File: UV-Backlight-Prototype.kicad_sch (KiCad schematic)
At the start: 82 parts, among them J1 Conn_02x08_Odd_Even

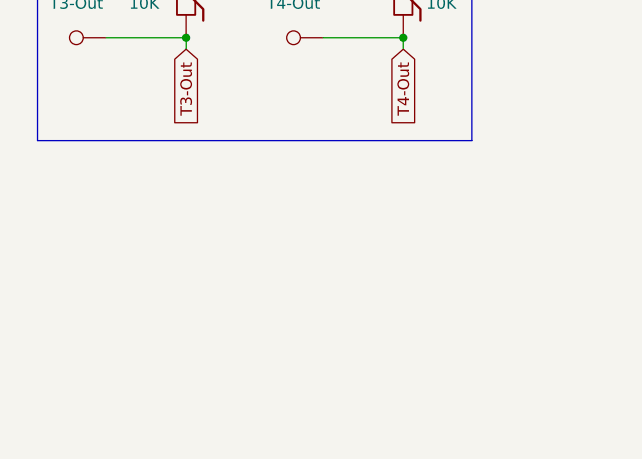
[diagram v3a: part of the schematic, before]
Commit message: Update UV-Backlight-Prototype.kicad_sch
Added Mounting holes to schematic. M3 mounting holes, connected to ground, vias around hole for aesthetics
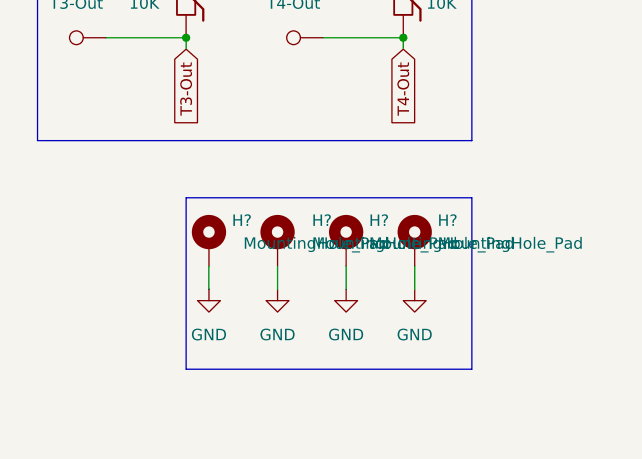
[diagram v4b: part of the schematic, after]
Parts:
- added H? (x3): MountingHole_Pad, MountingHole:MountingHole_3.2mm_M3_Pad_Via, symbol Mechanical:MountingHole_Pad
- added H?: MountingHole_Pad, symbol Mechanical:MountingHole_Pad
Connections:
- new net GND: H?.1, H?.1, H?.1, H?.1
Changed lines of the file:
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@@
+    (stroke (width 0) (type default) (color 0 0 0 0))
+  )
+  (wire (pts (xy 255.27 139.7) (xy 255.27 142.24))
     (stroke (width 0) (type default) (color 0 0 0 0))
   )
@@
     (stroke (width 0) (type default) (color 0 0 0 0))
   )
+  (polyline (pts (xy 261.62 132.08) (xy 261.62 151.13))
+    (stroke (width 0) (type default) (color 0 0 0 0))
+  )
   (wire (pts (xy 229.87 40.64) (xy 237.49 40.64))
     (stroke (width 0) (type default) (color 0 0 0 0))
@@
     (stroke (width 0) (type default) (color 0 0 0 0))
   )
+  (polyline (pts (xy 229.87 132.08) (xy 229.87 151.13))
+    (stroke (width 0) (type default) (color 0 0 0 0))
+  )
   (wire (pts (xy 97.79 53.34) (xy 97.79 55.88))
     (stroke (width 0) (type default) (color 0 0 0 0))
@@
     (stroke (width 0) (type default) (color 0 0 0 0))
   )
+  (wire (pts (xy 232.41 139.7) (xy 232.41 142.24))
+    (stroke (width 0) (type default) (color 0 0 0 0))
+  )
   (polyline (pts (xy 213.36 57.15) (xy 261.62 57.15))
     (stroke (width 0) (type default) (color 0 0 0 0))
@@
     (stroke (width 0) (type default) (color 0 0 0 0))
   )
+  (wire (pts (xy 240.03 139.7) (xy 240.03 142.24))
+    (stroke (width 0) (type default) (color 0 0 0 0))
+  )
   (wire (pts (xy 149.86 123.19) (xy 151.13 123.19))
     (stroke (width 0) (type default) (color 0 0 0 0))
@@
     (stroke (width 0) (type default) (color 0 0 0 0))
   )
+  (wire (pts (xy 247.65 139.7) (xy 247.65 142.24))
+    (stroke (width 0) (type default) (color 0 0 0 0))
+  )
   (wire (pts (xy 44.45 107.95) (xy 44.45 109.22))
     (stroke (width 0) (type default) (color 0 0 0 0))
@@
     (stroke (width 0) (type default) (color 0 0 0 0))
   )
+  (polyline (pts (xy 261.62 151.13) (xy 229.87 151.13))
+    (stroke (width 0) (type default) (color 0 0 0 0))
+  )
   (polyline (pts (xy 261.62 57.15) (xy 261.62 125.73))
     (stroke (width 0) (type default) (color 0 0 0 0))
@@
   )
   (polyline (pts (xy 274.32 54.61) (xy 213.36 54.61))
+    (stroke (width 0) (type default) (color 0 0 0 0))
+  )
+  (polyline (pts (xy 229.87 132.08) (xy 261.62 132.08))
     (stroke (width 0) (type default) (color 0 0 0 0))
   )
@@
     (pin "1")
   )
+  (symbol (lib_id "power:GND") (at 255.27 142.24 0) (unit 1)
+    (in_bom yes) (on_board yes) (fields_autoplaced)
+    (property "Reference" "#PWR?" (id 0) (at 255.27 148.59 0)
+      (effects (font (size 1.27 1.27)) hide)
+    )
+    (property "Value" "GND" (id 1) (at 255.27 147.32 0))
+    (property "Footprint" "" (id 2) (at 255.27 142.24 0)
+      (effects (font (size 1.27 1.27)) hide)
+    )
+    (property "Datasheet" "" (id 3) (at 255.27 142.24 0)
+      (effects (font (size 1.27 1.27)) hide)
+    )
+    (pin "1")
+  )
   (symbol (lib_id "Jumper:Jumper_2_Open") (at 142.24 33.02 0) (unit 1)
     (in_bom yes) (on_board yes)
@@
     (pin "2")
   )
+  (symbol (lib_id "Mechanical:MountingHole_Pad") (at 247.65 137.16 0) (unit 1)
+    (in_bom yes) (on_board yes) (fields_autoplaced)
+    (property "Reference" "H?" (id 0) (at 250.19 134.6199 0)
+      (effects (font (size 1.27 1.27)) (justify left))
+    )
+    (property "Value" "MountingHole_Pad" (id 1) (at 250.19 137.1599 0)
+      (effects (font (size 1.27 1.27)) (justify left))
+    )
+    (property "Footprint" "MountingHole:MountingHole_3.2mm_M3_Pad_Via" (id 2) (at 247.65 137.16 0)
+      (effects (font (size 1.27 1.27)) hide)
+    )
+    (property "Datasheet" "~" (id 3) (at 247.65 137.16 0)
+      (effects (font (size 1.27 1.27)) hide)
+    )
+    (pin "1")
+  )
   (symbol (lib_id "Jumper:Jumper_2_Open") (at 90.17 33.02 0) (unit 1)
     (in_bom yes) (on_board yes)
@@
     (pin "1")
   )
+  (symbol (lib_id "Mechanical:MountingHole_Pad") (at 255.27 137.16 0) (unit 1)
+    (in_bom yes) (on_board yes) (fields_autoplaced)
+    (property "Reference" "H?" (id 0) (at 257.81 134.6199 0)
+      (effects (font (size 1.27 1.27)) (justify left))
+    )
+    (property "Value" "MountingHole_Pad" (id 1) (at 257.81 137.1599 0)
+      (effects (font (size 1.27 1.27)) (justify left))
+    )
+    (property "Footprint" "MountingHole:MountingHole_3.2mm_M3_Pad_Via" (id 2) (at 255.27 137.16 0)
+      (effects (font (size 1.27 1.27)) hide)
+    )
+    (property "Datasheet" "~" (id 3) (at 255.27 137.16 0)
+      (effects (font (size 1.27 1.27)) hide)
+    )
+    (pin "1")
+  )
   (symbol (lib_id "Connector:TestPoint") (at 97.79 31.75 270) (unit 1)
     (in_bom yes) (on_board yes) (fields_autoplaced)
@@
     (pin "2")
   )
+  (symbol (lib_id "Mechanical:MountingHole_Pad") (at 232.41 137.16 0) (unit 1)
+    (in_bom yes) (on_board yes)
+    (property "Reference" "H?" (id 0) (at 234.95 134.6199 0)
+      (effects (font (size 1.27 1.27)) (justify left))
+    )
+    (property "Value" "MountingHole_Pad" (id 1) (at 236.22 137.1599 0)
+      (effects (font (size 1.27 1.27)) (justify left))
+    )
+    (property "Footprint" "" (id 2) (at 232.41 137.16 0)
+      (effects (font (size 1.27 1.27)) hide)
+    )
+    (property "Datasheet" "~" (id 3) (at 232.41 137.16 0)
+      (effects (font (size 1.27 1.27)) hide)
+    )
+    (pin "1")
+  )
   (symbol (lib_id "Connector:TestPoint") (at 151.13 93.98 270) (unit 1)
     (in_bom yes) (on_board yes) (fields_autoplaced)
@@
     (pin "2")
   )
+  (symbol (lib_id "power:GND") (at 240.03 142.24 0) (unit 1)
+    (in_bom yes) (on_board yes) (fields_autoplaced)
+    (property "Reference" "#PWR?" (id 0) (at 240.03 148.59 0)
+      (effects (font (size 1.27 1.27)) hide)
+    )
+    (property "Value" "GND" (id 1) (at 240.03 147.32 0))
+    (property "Footprint" "" (id 2) (at 240.03 142.24 0)
+      (effects (font (size 1.27 1.27)) hide)
+    )
+    (property "Datasheet" "" (id 3) (at 240.03 142.24 0)
+      (effects (font (size 1.27 1.27)) hide)
+    )
+    (pin "1")
+  )
   (symbol (lib_id "Connector:TestPoint") (at 245.11 81.28 90) (unit 1)
     (in_bom yes) (on_board yes) (fields_autoplaced)
@@
     (pin "2")
   )
+  (symbol (lib_id "power:GND") (at 232.41 142.24 0) (unit 1)
+    (in_bom yes) (on_board yes) (fields_autoplaced)
+    (property "Reference" "#PWR?" (id 0) (at 232.41 148.59 0)
+      (effects (font (size 1.27 1.27)) hide)
+    )
+    (property "Value" "GND" (id 1) (at 232.41 147.32 0))
+    (property "Footprint" "" (id 2) (at 232.41 142.24 0)
+      (effects (font (size 1.27 1.27)) hide)
+    )
+    (property "Datasheet" "" (id 3) (at 232.41 142.24 0)
+      (effects (font (size 1.27 1.27)) hide)
+    )
+    (pin "1")
+  )
   (symbol (lib_id "Device:LED") (at 44.45 102.87 90) (unit 1)
     (in_bom yes) (on_board yes) (fields_autoplaced)
@@
     (pin "1")
     (pin "2")
+  )
+  (symbol (lib_id "power:GND") (at 247.65 142.24 0) (unit 1)
+    (in_bom yes) (on_board yes) (fields_autoplaced)
+    (property "Reference" "#PWR?" (id 0) (at 247.65 148.59 0)
+      (effects (font (size 1.27 1.27)) hide)
+    )
+    (property "Value" "GND" (id 1) (at 247.65 147.32 0))
+    (property "Footprint" "" (id 2) (at 247.65 142.24 0)
+      (effects (font (size 1.27 1.27)) hide)
+    )
+    (property "Datasheet" "" (id 3) (at 247.65 142.24 0)
+      (effects (font (size 1.27 1.27)) hide)
+    )
+    (pin "1")
   )
   (symbol (lib_id "Connector:TestPoint") (at 151.13 106.68 270) (unit 1)
@@
     (pin "2")
   )
+  (symbol (lib_id "Mechanical:MountingHole_Pad") (at 240.03 137.16 0) (unit 1)
+    (in_bom yes) (on_board yes)
+    (property "Reference" "H?" (id 0) (at 243.84 134.6199 0)
+      (effects (font (size 1.27 1.27)) (justify left))
+    )
+    (property "Value" "MountingHole_Pad" (id 1) (at 243.84 137.1599 0)
+      (effects (font (size 1.27 1.27)) (justify left))
+    )
+    (property "Footprint" "MountingHole:MountingHole_3.2mm_M3_Pad_Via" (id 2) (at 240.03 137.16 0)
+      (effects (font (size 1.27 1.27)) hide)
+    )
+    (property "Datasheet" "~" (id 3) (at 240.03 137.16 0)
+      (effects (font (size 1.27 1.27)) hide)
+    )
+    (pin "1")
+  )
   (symbol (lib_id "Connector:TestPoint") (at 220.98 71.12 90) (unit 1)
     (in_bom yes) (on_board yes) (fields_autoplaced)
@@
   )
   (symbol_instances
+    (path "/1281690f-d0c0-4e7c-8e9b-b3fec11a3e67"
+      (reference "#PWR?") (unit 1) (value "GND") (footprint "")
+    )
+    (path "/9259b80d-1969-4589-94a9-080673952826"
+      (reference "#PWR?") (unit 1) (value "GND") (footprint "")
+    )
+    (path "/a3a27186-2051-4909-991d-caf80cec8df9"
+      (reference "#PWR?") (unit 1) (value "GND") (footprint "")
+    )
+    (path "/bb1469d3-6926-4d46-adfc-865ef7215321"
+      (reference "#PWR?") (unit 1) (value "GND") (footprint "")
+    )
     (path "/dce51636-b20e-418f-aae8-16711401d173"
       (reference "D1") (unit 1) (value "UV LED") (footprint "LED_SMD:LED_PLCC_2835_Handsoldering")
@@
       (reference "D21") (unit 1) (value "UV LED") (footprint "LED_SMD:LED_PLCC_2835_Handsoldering")
     )
+    (path "/358db39b-417f-4d50-8276-ae73a4dbda31"
+      (reference "H?") (unit 1) (value "MountingHole_Pad") (footprint "MountingHole:MountingHole_3.2mm_M3_Pad_Via")
+    )
+    (path "/40150b75-969d-4cd4-93e5-e8258fa7d188"
+      (reference "H?") (unit 1) (value "MountingHole_Pad") (footprint "MountingHole:MountingHole_3.2mm_M3_Pad_Via")
+    )
+    (path "/757c54d8-07ff-441d-be3d-65751b9d4914"
+      (reference "H?") (unit 1) (value "MountingHole_Pad") (footprint "MountingHole:MountingHole_3.2mm_M3_Pad_Via")
+    )
+    (path "/e24b16b7-83bf-4189-99e5-84cfc419f98d"
+      (reference "H?") (unit 1) (value "MountingHole_Pad") (footprint "MountingHole:MountingHole_3.2mm_M3_Pad_Via")
+    )
     (path "/c36a3340-352f-453e-a7ed-e92b15cd9612"

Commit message: Autosave
autosave
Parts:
- gave numbers to parts that had none: 4
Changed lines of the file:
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@@
   (symbol (lib_id "power:GND") (at 255.27 142.24 0) (unit 1)
     (in_bom yes) (on_board yes) (fields_autoplaced)
-    (property "Reference" "#PWR?" (id 0) (at 255.27 148.59 0)
+    (property "Reference" "#PWR04" (id 0) (at 255.27 148.59 0)
       (effects (font (size 1.27 1.27)) hide)
     )
@@
   (symbol (lib_id "Mechanical:MountingHole_Pad") (at 247.65 137.16 0) (unit 1)
     (in_bom yes) (on_board yes) (fields_autoplaced)
-    (property "Reference" "H?" (id 0) (at 250.19 134.6199 0)
+    (property "Reference" "H3" (id 0) (at 250.19 134.6199 0)
       (effects (font (size 1.27 1.27)) (justify left))
     )
@@
   (symbol (lib_id "Mechanical:MountingHole_Pad") (at 255.27 137.16 0) (unit 1)
     (in_bom yes) (on_board yes) (fields_autoplaced)
-    (property "Reference" "H?" (id 0) (at 257.81 134.6199 0)
+    (property "Reference" "H4" (id 0) (at 257.81 134.6199 0)
       (effects (font (size 1.27 1.27)) (justify left))
     )
@@
   (symbol (lib_id "Mechanical:MountingHole_Pad") (at 232.41 137.16 0) (unit 1)
     (in_bom yes) (on_board yes)
-    (property "Reference" "H?" (id 0) (at 234.95 134.6199 0)
+    (property "Reference" "H1" (id 0) (at 234.95 134.6199 0)
       (effects (font (size 1.27 1.27)) (justify left))
     )
@@
   (symbol (lib_id "power:GND") (at 240.03 142.24 0) (unit 1)
     (in_bom yes) (on_board yes) (fields_autoplaced)
-    (property "Reference" "#PWR?" (id 0) (at 240.03 148.59 0)
+    (property "Reference" "#PWR02" (id 0) (at 240.03 148.59 0)
       (effects (font (size 1.27 1.27)) hide)
     )
@@
   (symbol (lib_id "power:GND") (at 232.41 142.24 0) (unit 1)
     (in_bom yes) (on_board yes) (fields_autoplaced)
-    (property "Reference" "#PWR?" (id 0) (at 232.41 148.59 0)
+    (property "Reference" "#PWR01" (id 0) (at 232.41 148.59 0)
       (effects (font (size 1.27 1.27)) hide)
     )
@@
   (symbol (lib_id "power:GND") (at 247.65 142.24 0) (unit 1)
     (in_bom yes) (on_board yes) (fields_autoplaced)
-    (property "Reference" "#PWR?" (id 0) (at 247.65 148.59 0)
+    (property "Reference" "#PWR03" (id 0) (at 247.65 148.59 0)
       (effects (font (size 1.27 1.27)) hide)
     )
@@
   (symbol (lib_id "Mechanical:MountingHole_Pad") (at 240.03 137.16 0) (unit 1)
     (in_bom yes) (on_board yes)
-    (property "Reference" "H?" (id 0) (at 243.84 134.6199 0)
+    (property "Reference" "H2" (id 0) (at 243.84 134.6199 0)
       (effects (font (size 1.27 1.27)) (justify left))
     )
@@
   )
   (symbol_instances
+    (path "/a3a27186-2051-4909-991d-caf80cec8df9"
+      (reference "#PWR01") (unit 1) (value "GND") (footprint "")
+    )
+    (path "/9259b80d-1969-4589-94a9-080673952826"
+      (reference "#PWR02") (unit 1) (value "GND") (footprint "")
+    )
+    (path "/bb1469d3-6926-4d46-adfc-865ef7215321"
+      (reference "#PWR03") (unit 1) (value "GND") (footprint "")
+    )
     (path "/1281690f-d0c0-4e7c-8e9b-b3fec11a3e67"
-      (reference "#PWR?") (unit 1) (value "GND") (footprint "")
-    )
-    (path "/9259b80d-1969-4589-94a9-080673952826"
-      (reference "#PWR?") (unit 1) (value "GND") (footprint "")
-    )
-    (path "/a3a27186-2051-4909-991d-caf80cec8df9"
-      (reference "#PWR?") (unit 1) (value "GND") (footprint "")
-    )
-    (path "/bb1469d3-6926-4d46-adfc-865ef7215321"
-      (reference "#PWR?") (unit 1) (value "GND") (footprint "")
+      (reference "#PWR04") (unit 1) (value "GND") (footprint "")
     )
     (path "/dce51636-b20e-418f-aae8-16711401d173"
@@
       (reference "D21") (unit 1) (value "UV LED") (footprint "LED_SMD:LED_PLCC_2835_Handsoldering")
     )
+    (path "/757c54d8-07ff-441d-be3d-65751b9d4914"
+      (reference "H1") (unit 1) (value "MountingHole_Pad") (footprint "MountingHole:MountingHole_3.2mm_M3_Pad_Via")
+    )
+    (path "/e24b16b7-83bf-4189-99e5-84cfc419f98d"
+      (reference "H2") (unit 1) (value "MountingHole_Pad") (footprint "MountingHole:MountingHole_3.2mm_M3_Pad_Via")
+    )
     (path "/358db39b-417f-4d50-8276-ae73a4dbda31"
-      (reference "H?") (unit 1) (value "MountingHole_Pad") (footprint "MountingHole:MountingHole_3.2mm_M3_Pad_Via")
+      (reference "H3") (unit 1) (value "MountingHole_Pad") (footprint "MountingHole:MountingHole_3.2mm_M3_Pad_Via")
     )
     (path "/40150b75-969d-4cd4-93e5-e8258fa7d188"
-      (reference "H?") (unit 1) (value "MountingHole_Pad") (footprint "MountingHole:MountingHole_3.2mm_M3_Pad_Via")
-    )
-    (path "/757c54d8-07ff-441d-be3d-65751b9d4914"
-      (reference "H?") (unit 1) (value "MountingHole_Pad") (footprint "MountingHole:MountingHole_3.2mm_M3_Pad_Via")
-    )
-    (path "/e24b16b7-83bf-4189-99e5-84cfc419f98d"
-      (reference "H?") (unit 1) (value "MountingHole_Pad") (footprint "MountingHole:MountingHole_3.2mm_M3_Pad_Via")
+      (reference "H4") (unit 1) (value "MountingHole_Pad") (footprint "MountingHole:MountingHole_3.2mm_M3_Pad_Via")
     )
     (path "/c36a3340-352f-453e-a7ed-e92b15cd9612"

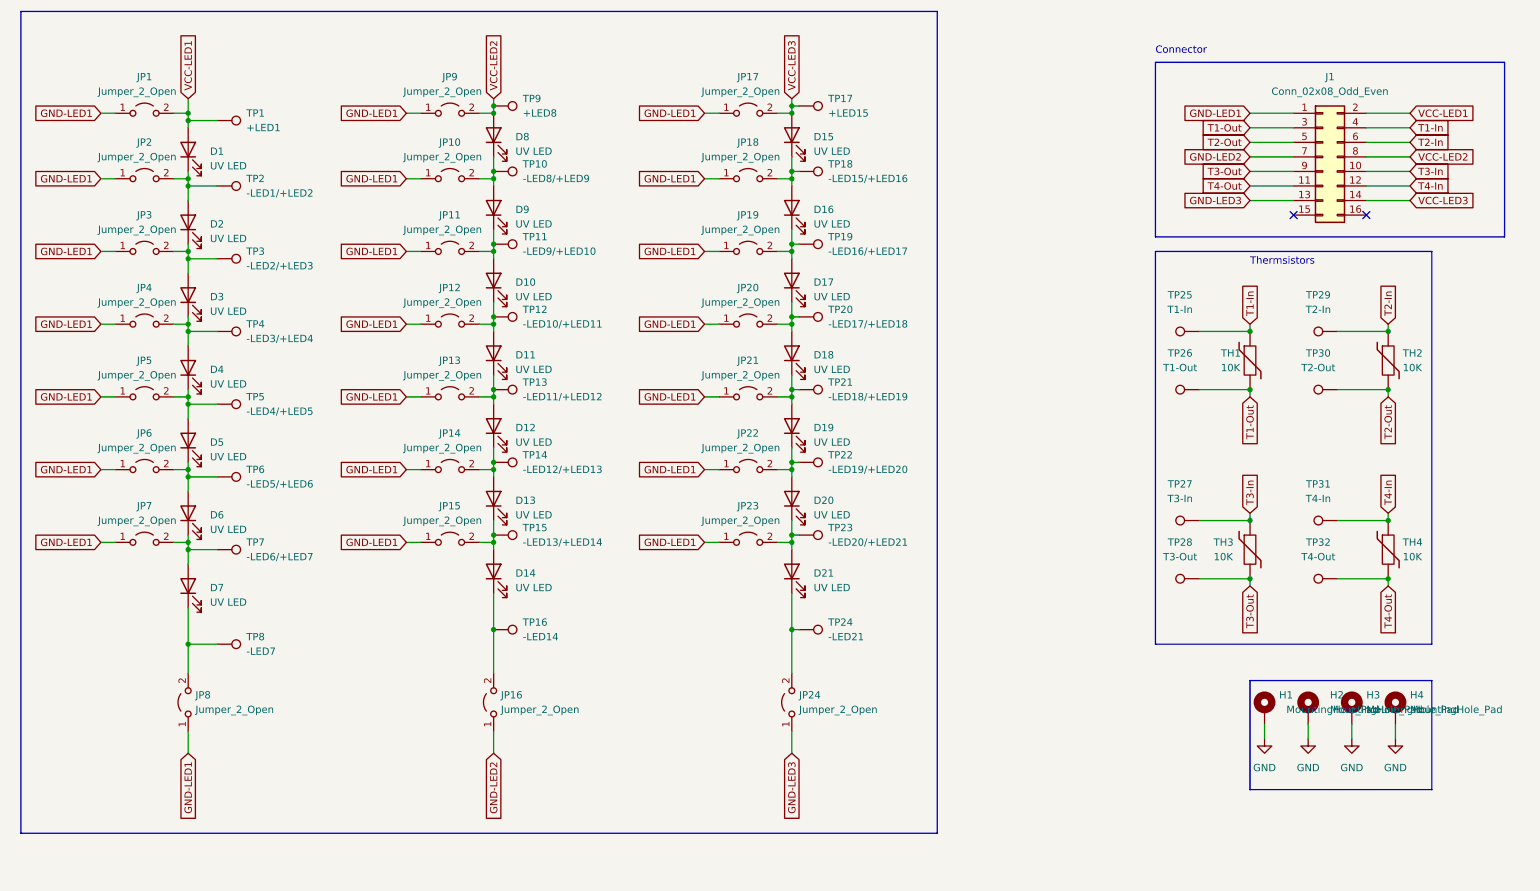
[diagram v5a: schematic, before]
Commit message: Progress Update
Changes to PCB:
Adjusted LED placement
Started Test point placement

Changes to schematic:
Test points for VCC and GND for LED strings 1,2,3 deemed redundant and removed.
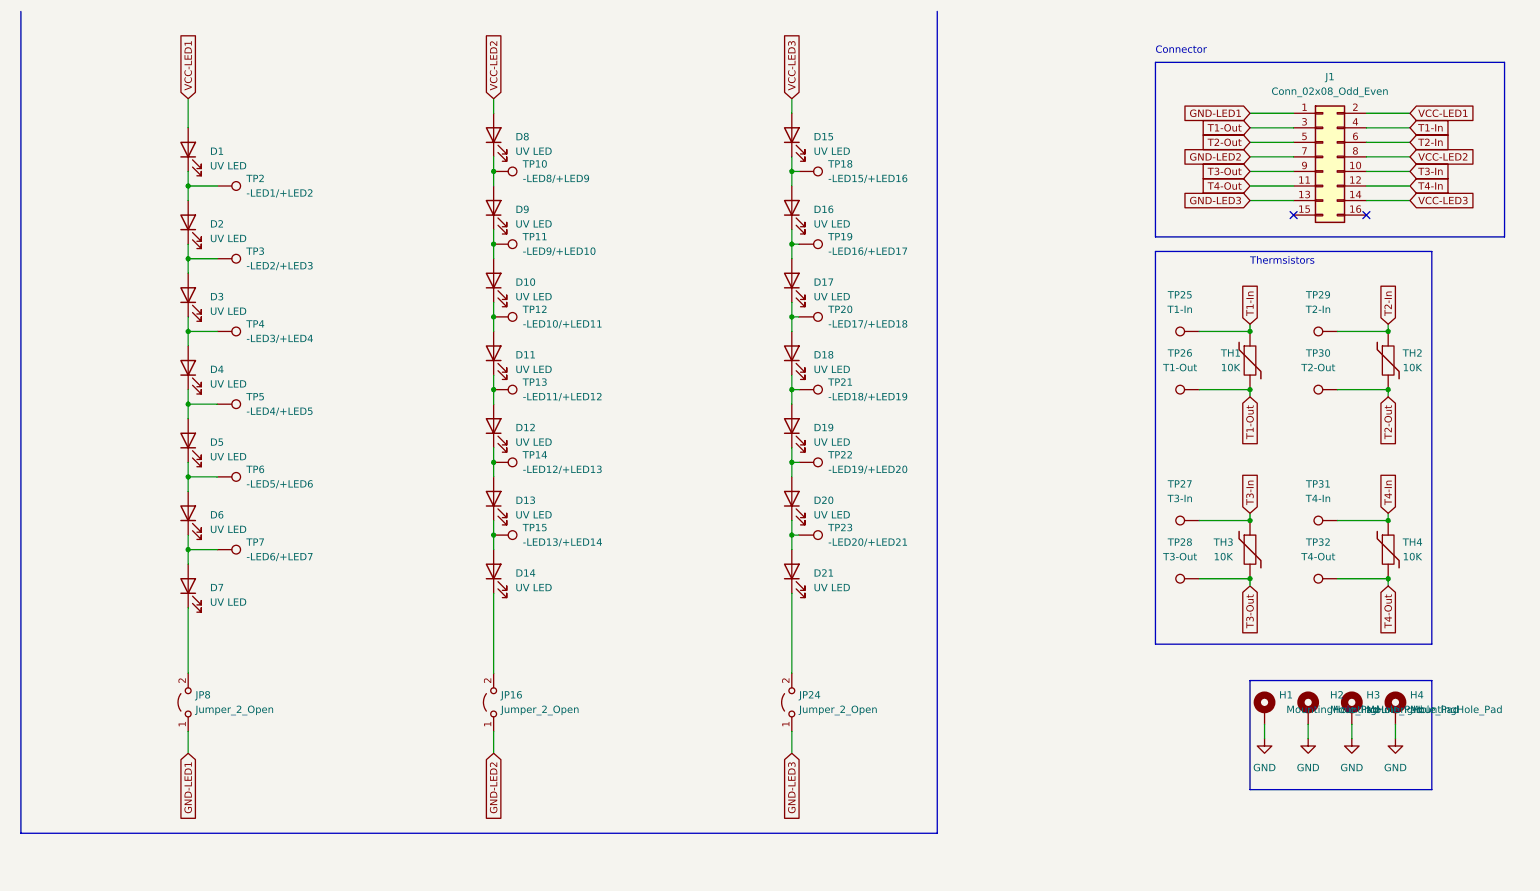
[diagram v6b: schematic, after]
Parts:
- removed JP1, JP10, JP11, JP12, JP13, JP14, JP15, JP17, JP18, JP19, JP2, JP20, JP21, JP22, JP23, JP3, JP4, JP5, JP6, JP7, JP9: Jumper_2_Open, Resistor_SMD:R_1206_3216Metric_Pad1.30x1.75mm_HandSolder, symbol Jumper:Jumper_2_Open
- removed TP1: +LED1, symbol Connector:TestPoint
- removed TP16: -LED14, TestPoint:TestPoint_Keystone_5000-5004_Miniature, symbol Connector:TestPoint
- removed TP17: +LED15, TestPoint:TestPoint_Keystone_5000-5004_Miniature, symbol Connector:TestPoint
- removed TP24: -LED21, TestPoint:TestPoint_Keystone_5000-5004_Miniature, symbol Connector:TestPoint
- removed TP8: -LED7, TestPoint:TestPoint_Keystone_5000-5004_Miniature, symbol Connector:TestPoint
- removed TP9: +LED8, TestPoint:TestPoint_Keystone_5000-5004_Miniature, symbol Connector:TestPoint
- H1: footprint (none) -> MountingHole:MountingHole_3.2mm_M3_Pad_Via
